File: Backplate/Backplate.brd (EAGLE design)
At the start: 230 x 110 mm, 29 parts, among them J1 USB_FTP, Q1 BQ2970, Q2 CSD16406Q3, Q3 CSD16406Q3, X1 Batt/Sun, X3 USB

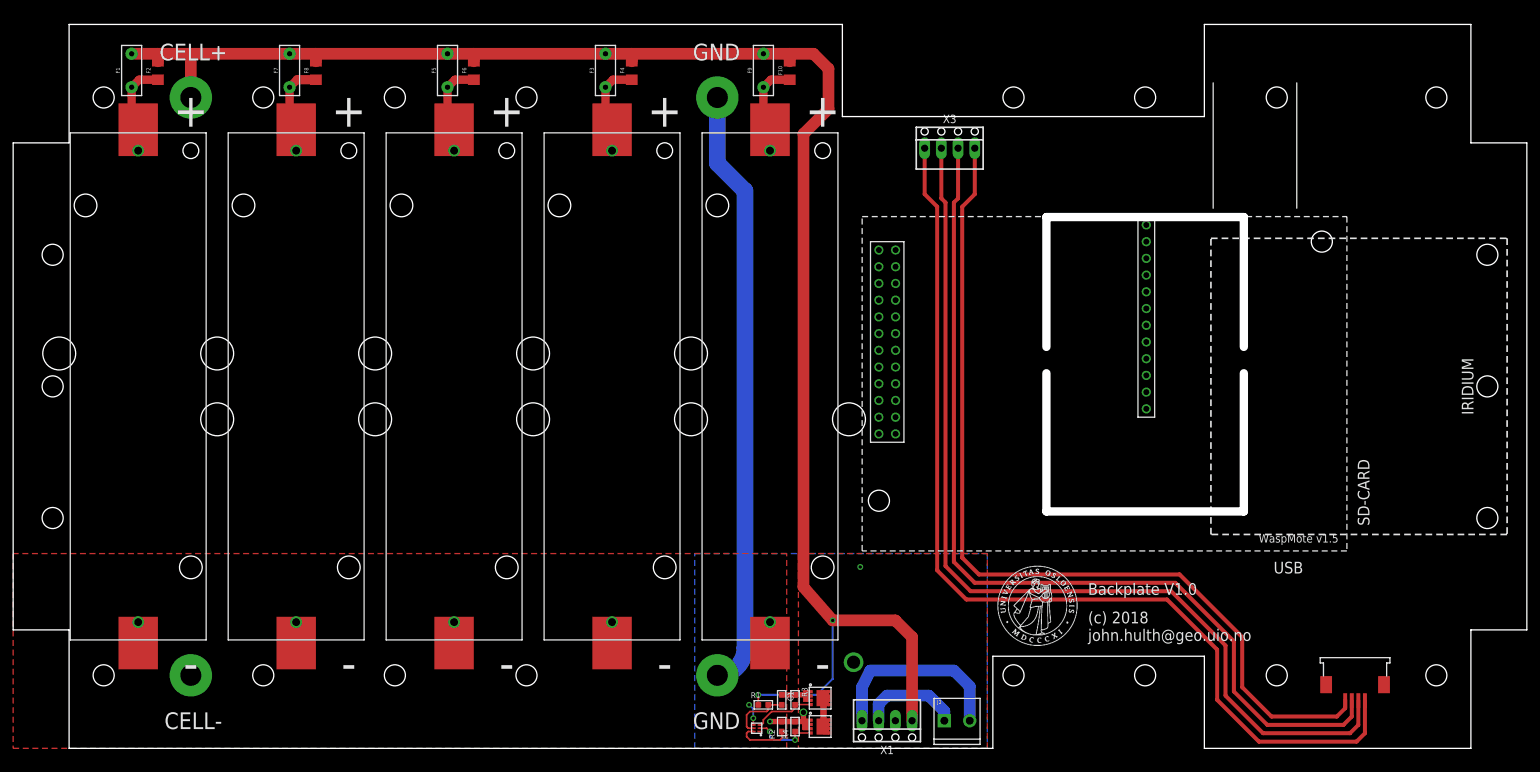
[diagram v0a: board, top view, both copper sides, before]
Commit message: Backplate v1.1 ordered
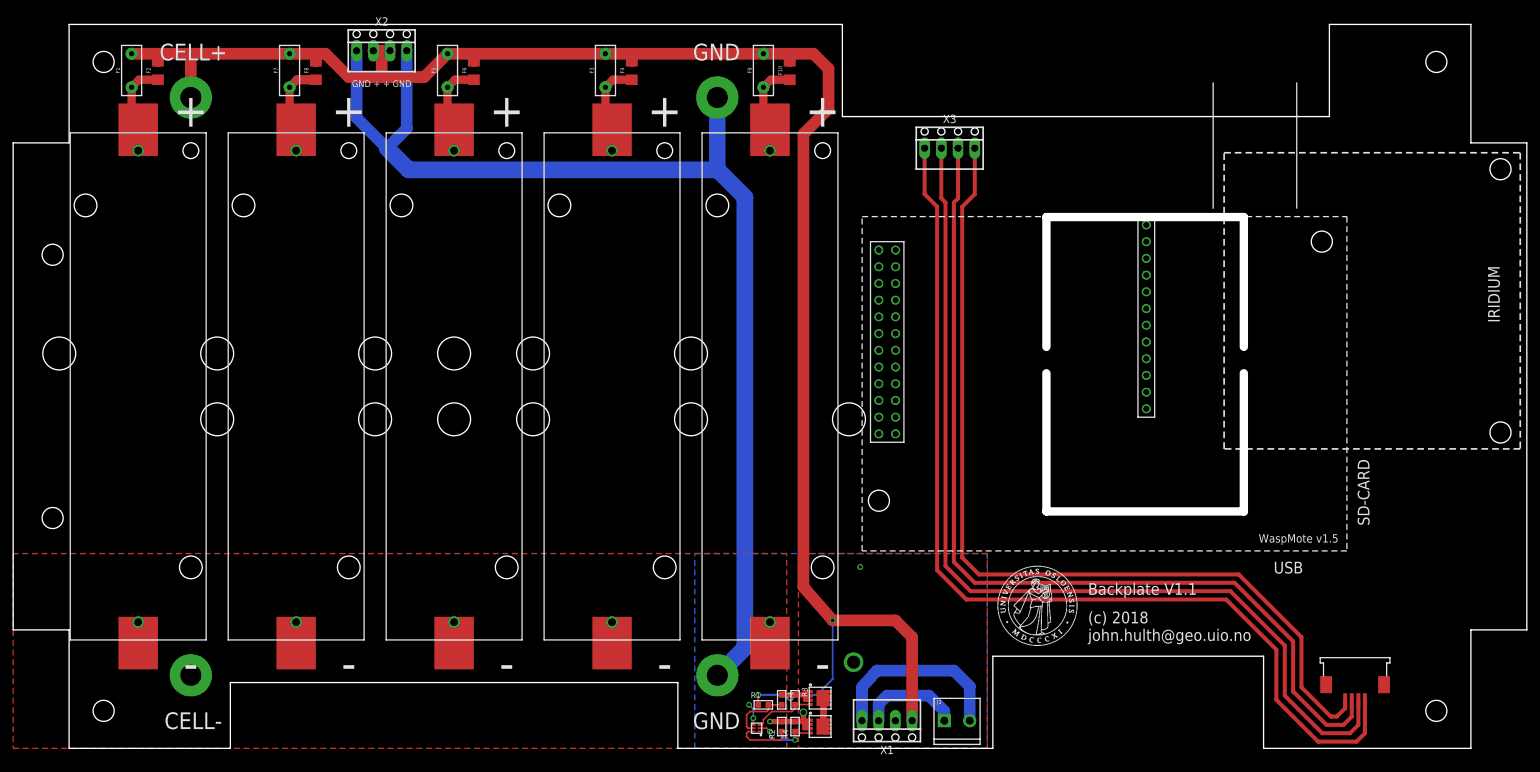
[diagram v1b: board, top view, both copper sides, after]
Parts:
- added X2: Batt Pack, con-molex:22-23-2041
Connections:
- net CELL+: now also X2.2, X2.3
- net GND: now also X2.1, X2.4
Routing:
- net GND: track 102.4 -> 186.7 mm
- net CELL+: track 255.1 -> 264.6 mm
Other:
- outline, holes or cut-outs redrawn
- board text added: "Backplate V1.1"
- board text added: "GND + + GND"
- board text removed: "Backplate V1.0"
